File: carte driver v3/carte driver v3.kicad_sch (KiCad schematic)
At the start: 50 parts, among them J1 UART CP, J10 STEPPER 2, J11 STEPPER 4, J2 UART BONUS, J3 conn 24v, J4 conn 5v, J5 ventilo, J6 STEPPER G, J7 STEPPER 1, J8 STEPPER 3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

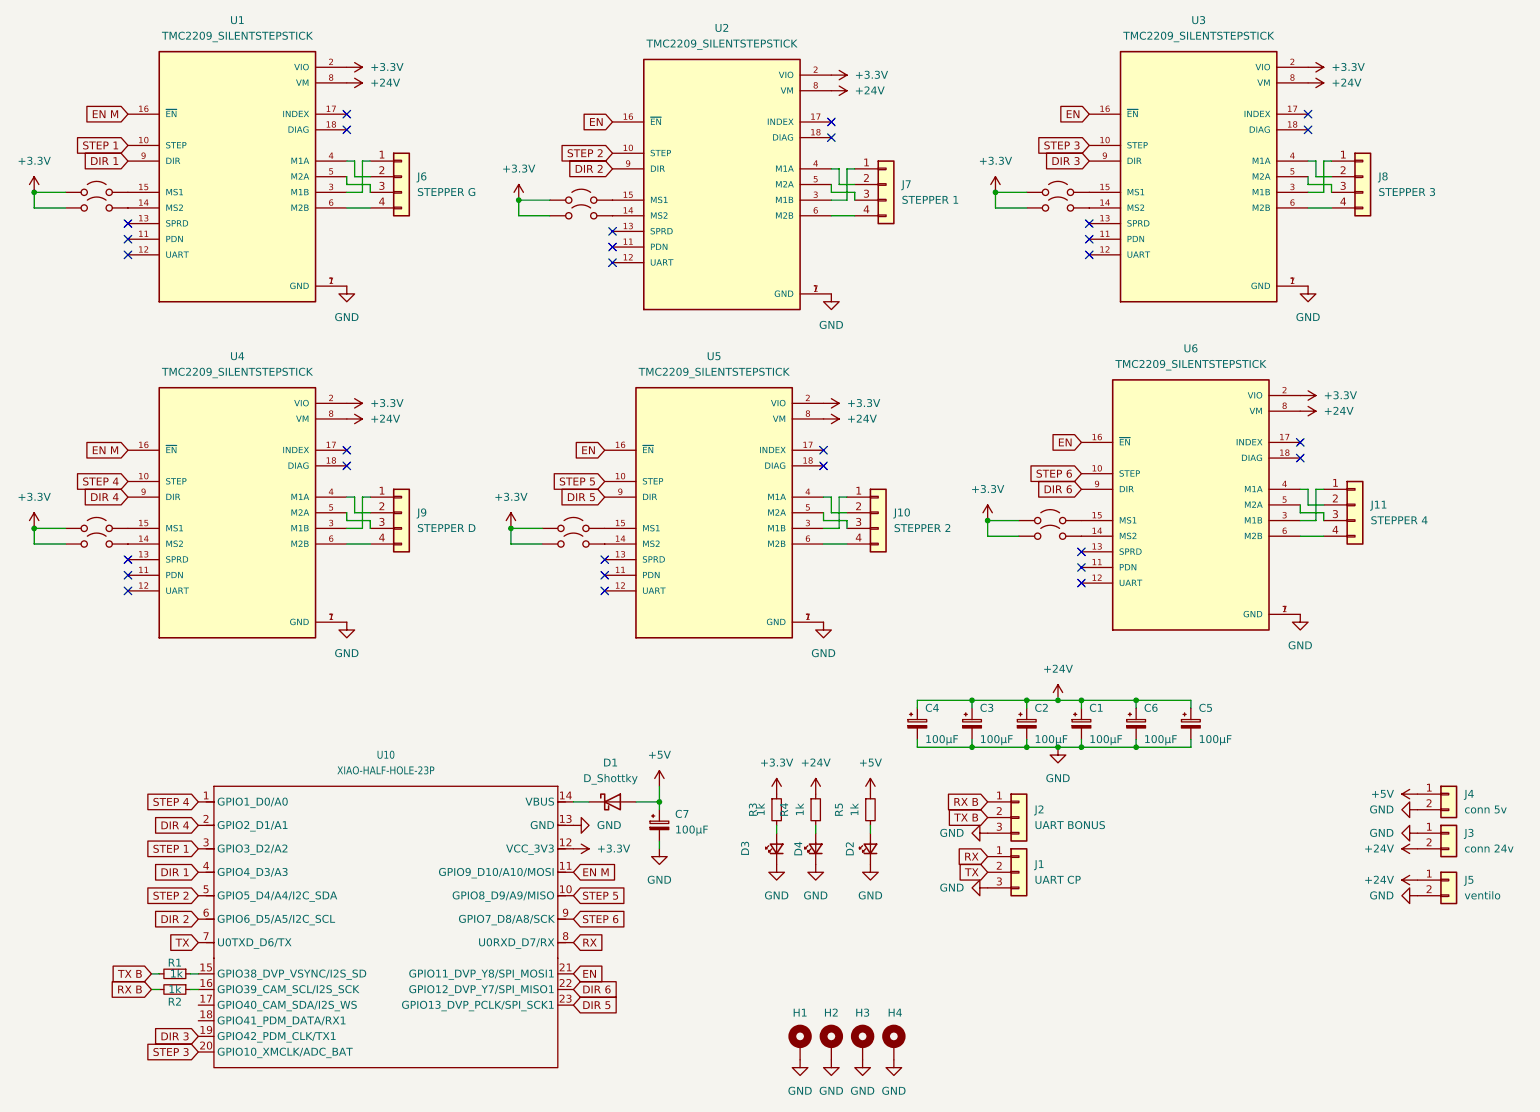
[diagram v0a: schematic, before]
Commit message: v3 fin routage
on espere que c'est le cas
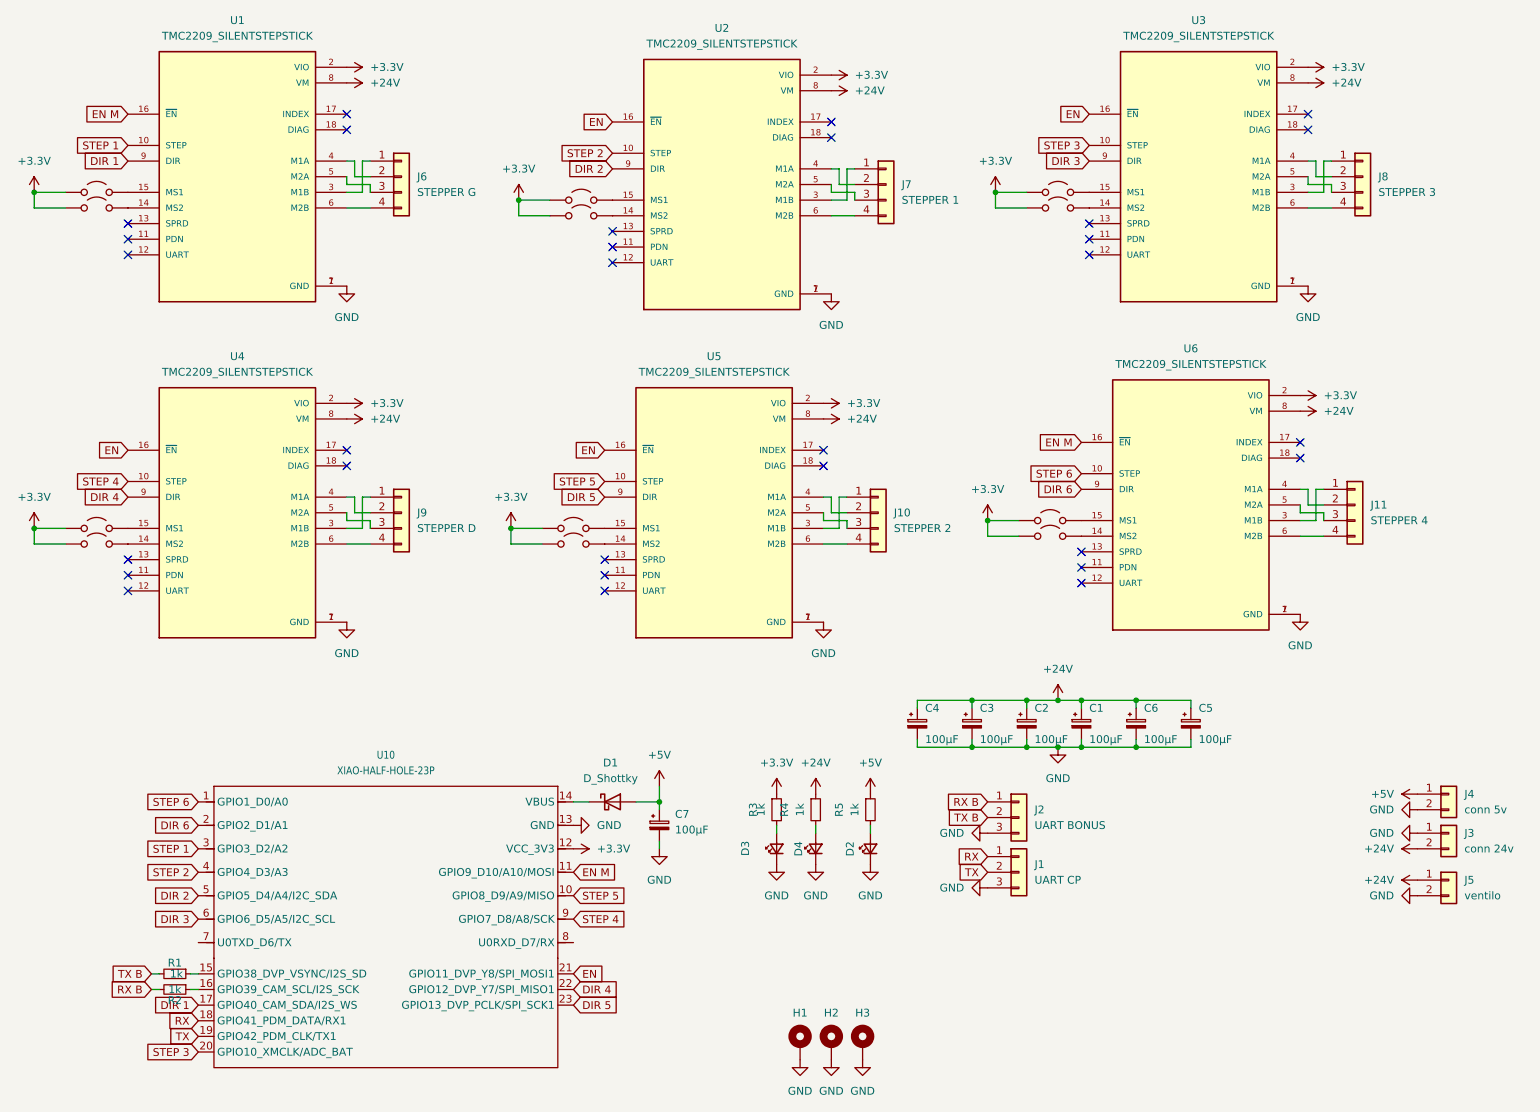
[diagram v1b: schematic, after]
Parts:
- removed H4: MountingHole_Pad, MountingHole:MountingHole_3.2mm_M3_Pad_Via, symbol Mechanical:MountingHole_Pad
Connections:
- net DIR 1: now also U10.17 (GPIO40_CAM_SDA/I2S_WS); no longer U10.4 (GPIO4_D3/A3)
- net DIR 2: now also U10.5 (GPIO5_D4/A4/I2C_SDA); no longer U10.6 (GPIO6_D5/A5/I2C_SCL)
- net DIR 3: now also U10.6 (GPIO6_D5/A5/I2C_SCL); no longer U10.19 (GPIO42_PDM_CLK/TX1)
- net DIR 4: now also U10.22 (GPIO12_DVP_Y7/SPI_MISO1); no longer U10.2 (GPIO2_D1/A1)
- net DIR 6: now also U10.2 (GPIO2_D1/A1); no longer U10.22 (GPIO12_DVP_Y7/SPI_MISO1)
- net EN: now also U4.16 (~{EN}); no longer U6.16 (~{EN})
- net EN M: now also U6.16 (~{EN}); no longer U4.16 (~{EN})
- net RX: now also U10.18 (GPIO41_PDM_DATA/RX1); no longer U10.8 (U0RXD_D7/RX)
- net STEP 2: now also U10.4 (GPIO4_D3/A3); no longer U10.5 (GPIO5_D4/A4/I2C_SDA)
- net STEP 4: now also U10.9 (GPIO7_D8/A8/SCK); no longer U10.1 (GPIO1_D0/A0)
- net STEP 6: now also U10.1 (GPIO1_D0/A0); no longer U10.9 (GPIO7_D8/A8/SCK)
- net TX: now also U10.19 (GPIO42_PDM_CLK/TX1); no longer U10.7 (U0TXD_D6/TX)
